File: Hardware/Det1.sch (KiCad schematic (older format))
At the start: 49 parts

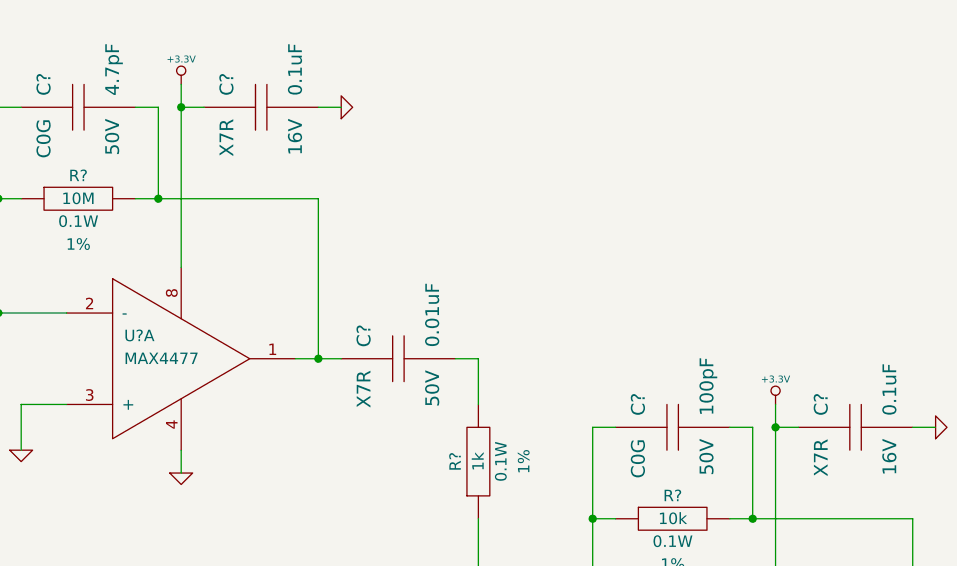
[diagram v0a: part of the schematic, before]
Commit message: Add LDO for analog
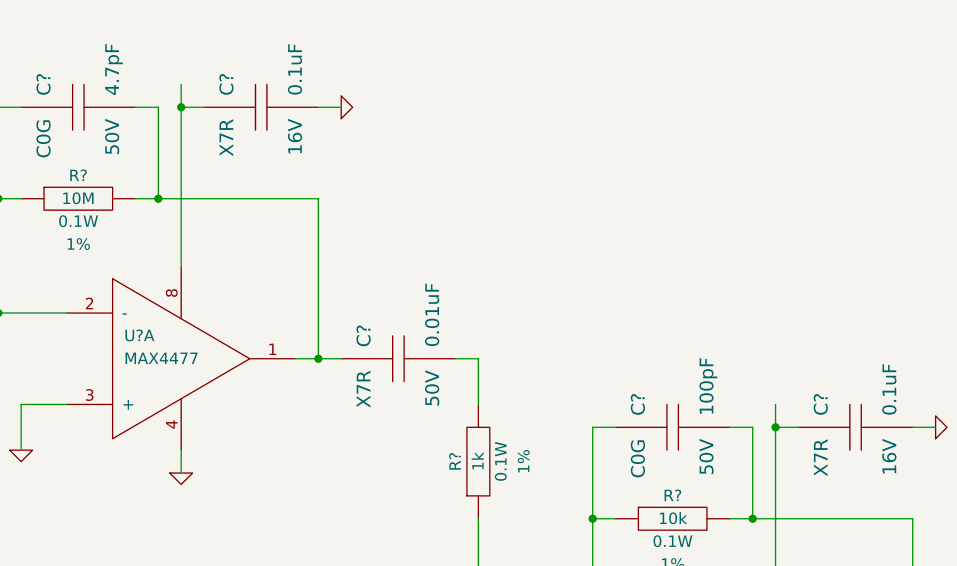
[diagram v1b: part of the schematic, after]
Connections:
- net labels removed: +3.3V
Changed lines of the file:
@@
 Sheet 2 5
 Title "Solid State Cosmic Ray Detector"
-Date "22 sep 2014"
+Date "23 sep 2014"
 Rev "1"
 Comp "Ethan Harstad"
@@
 $EndComp
 $Comp
-L +3.3V #PWR?
-U 1 1 52B91461
-P 6200 900
-F 0 "#PWR?" H 6200 860 30  0001 C CNN
-F 1 "+3.3V" H 6200 1010 30  0000 C CNN
-F 2 "" H 6200 900 60  0000 C CNN
-F 3 "" H 6200 900 60  0000 C CNN
-	1    6200 900
-	1    0    0    -1
-$EndComp
-$Comp
 L C C?
 U 1 1 52B91483
@@
 	0    -1   -1   0
 $EndComp
-$Comp
-L +3.3V #PWR?
-U 1 1 52B920B5
-P 8800 2300
-F 0 "#PWR?" H 8800 2260 30  0001 C CNN
-F 1 "+3.3V" H 8800 2410 30  0000 C CNN
-F 2 "" H 8800 2300 60  0000 C CNN
-F 3 "" H 8800 2300 60  0000 C CNN
-	1    8800 2300
-	1    0    0    -1
-$EndComp
-Wire Wire Line
+Wire Wire Line

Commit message: New detector chain
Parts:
- removed C? (x2): 4.7pF, CAPC1608, symbol C
- removed C? (x2): 0.1uF, CAPC1608, symbol C
- removed C? (x4): 0.01uF, CAPC1608, symbol C
- removed C? (x3): 100pF, CAPC1608, symbol C
- removed R? (x2): 10M, RESC1608, symbol R
- removed R? (x4): 1k, RESC1608, symbol R
- removed R? (x3): 10k, RESC1608, symbol R
- removed U? (x5): MAX4477, symbol OPAMP-DUAL
- added C? (x4): C, ~, symbol C
- added C? (x3): 0.1uF, CAPC1608, symbol C
- added C? (x2): 0.01uF, CAPC1608, symbol C
- added R? (x7): R, ~, symbol R
- added U? (x5): OPAMP-DUAL, ~, symbol OPAMP-DUAL
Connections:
- net labels added: VAA, VCOM
- net labels removed: +12V
- wire segments 116 -> 103
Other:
- note added: "Charge Amplifier"
- note added: "Differentiator Amplifier"
- note added: "Integrator Amplifier"

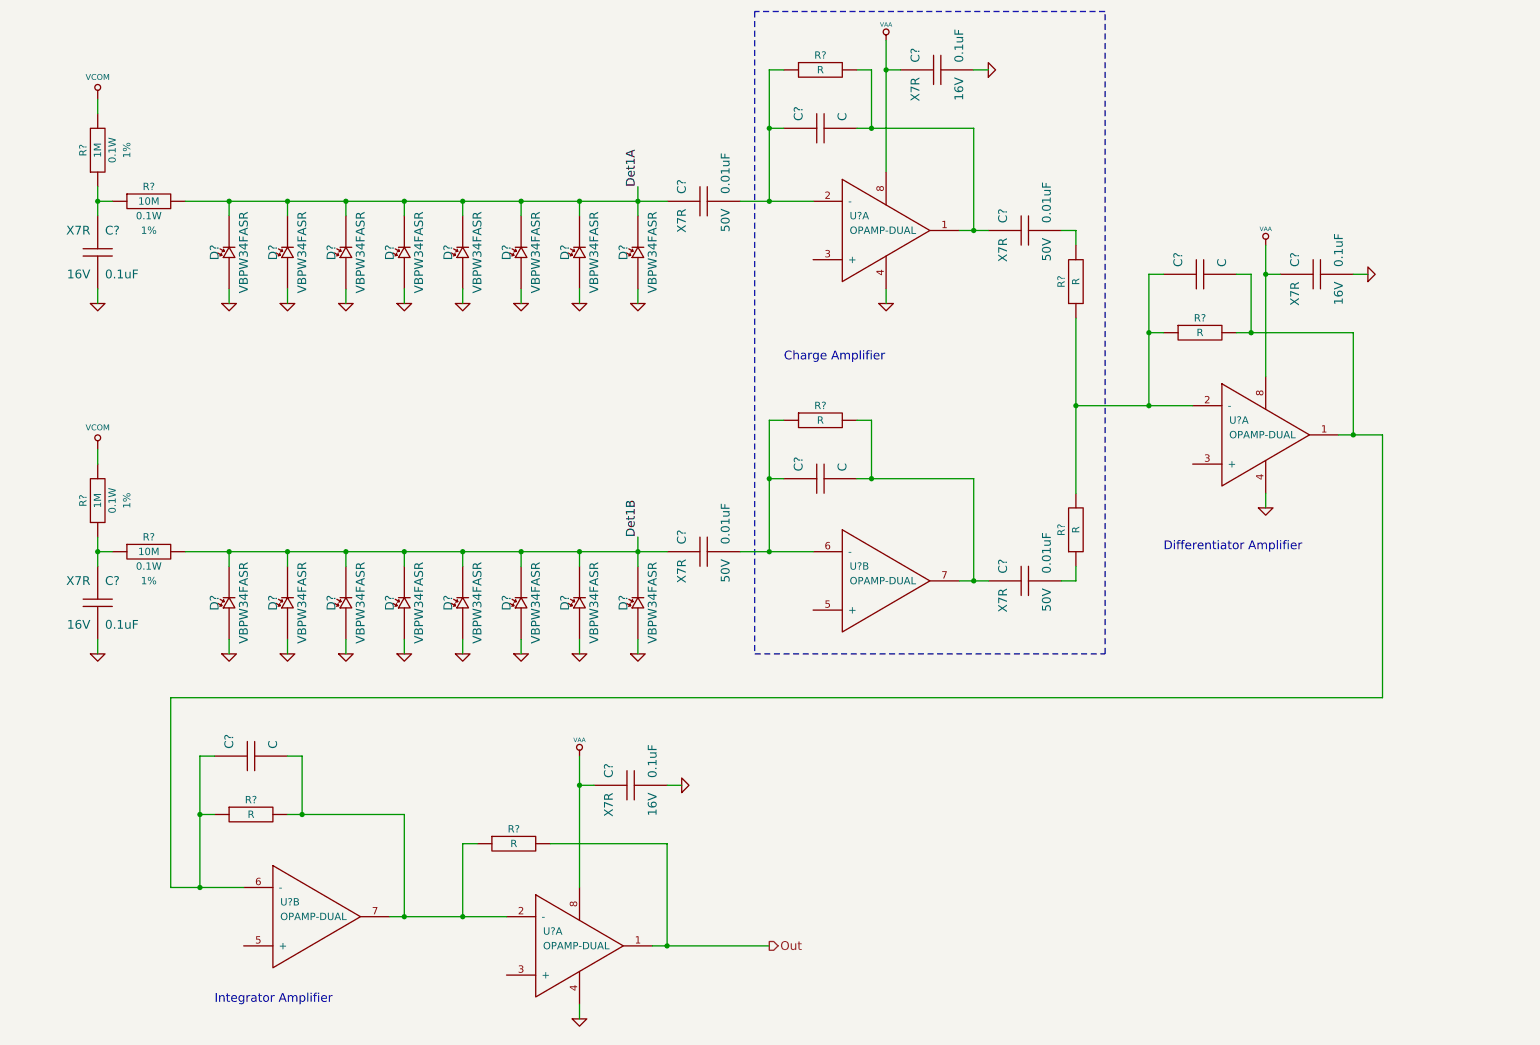
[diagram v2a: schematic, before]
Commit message: Rearrange detector chain
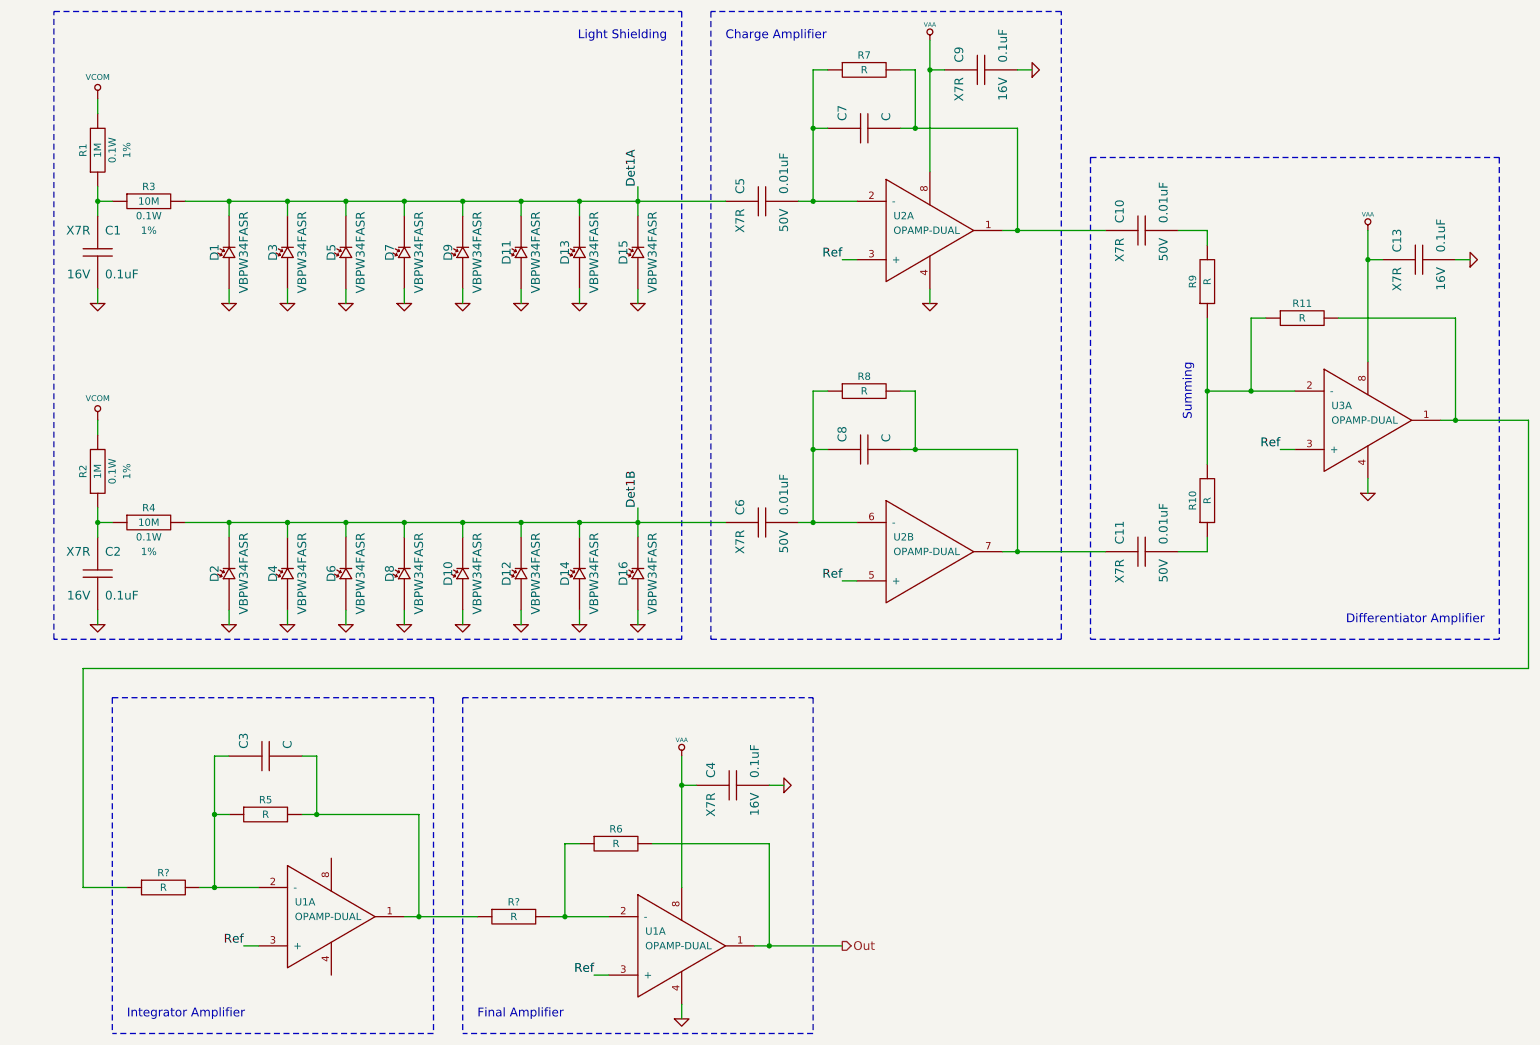
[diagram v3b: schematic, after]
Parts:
- removed C?: C, ~, symbol C
- added R? (x2): R, ~, symbol R
- gave numbers to parts that had none: 42
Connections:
- net Ref: now reaches U2.3 (+)
- net Ref: now also U1.3 (+), U1.3 (+), U2.5 (+), U3.3 (+)
- new net: R11.2, R?.1, U3.1
- new net: C3.2, R5.2, R?.1, U1.1
- new net: C3.1, R5.1, R?.2, U1.2 (-)
- new net: R6.1, R?.2, U1.2 (-)
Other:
- note added: "Final Amplifier"
- note added: "Light Shielding"
- note added: "Summing"
- moved on the sheet: C10, C11, C13, C2, C3, C4, C5, C6, C7, C8, C9, D10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

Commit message: Component values
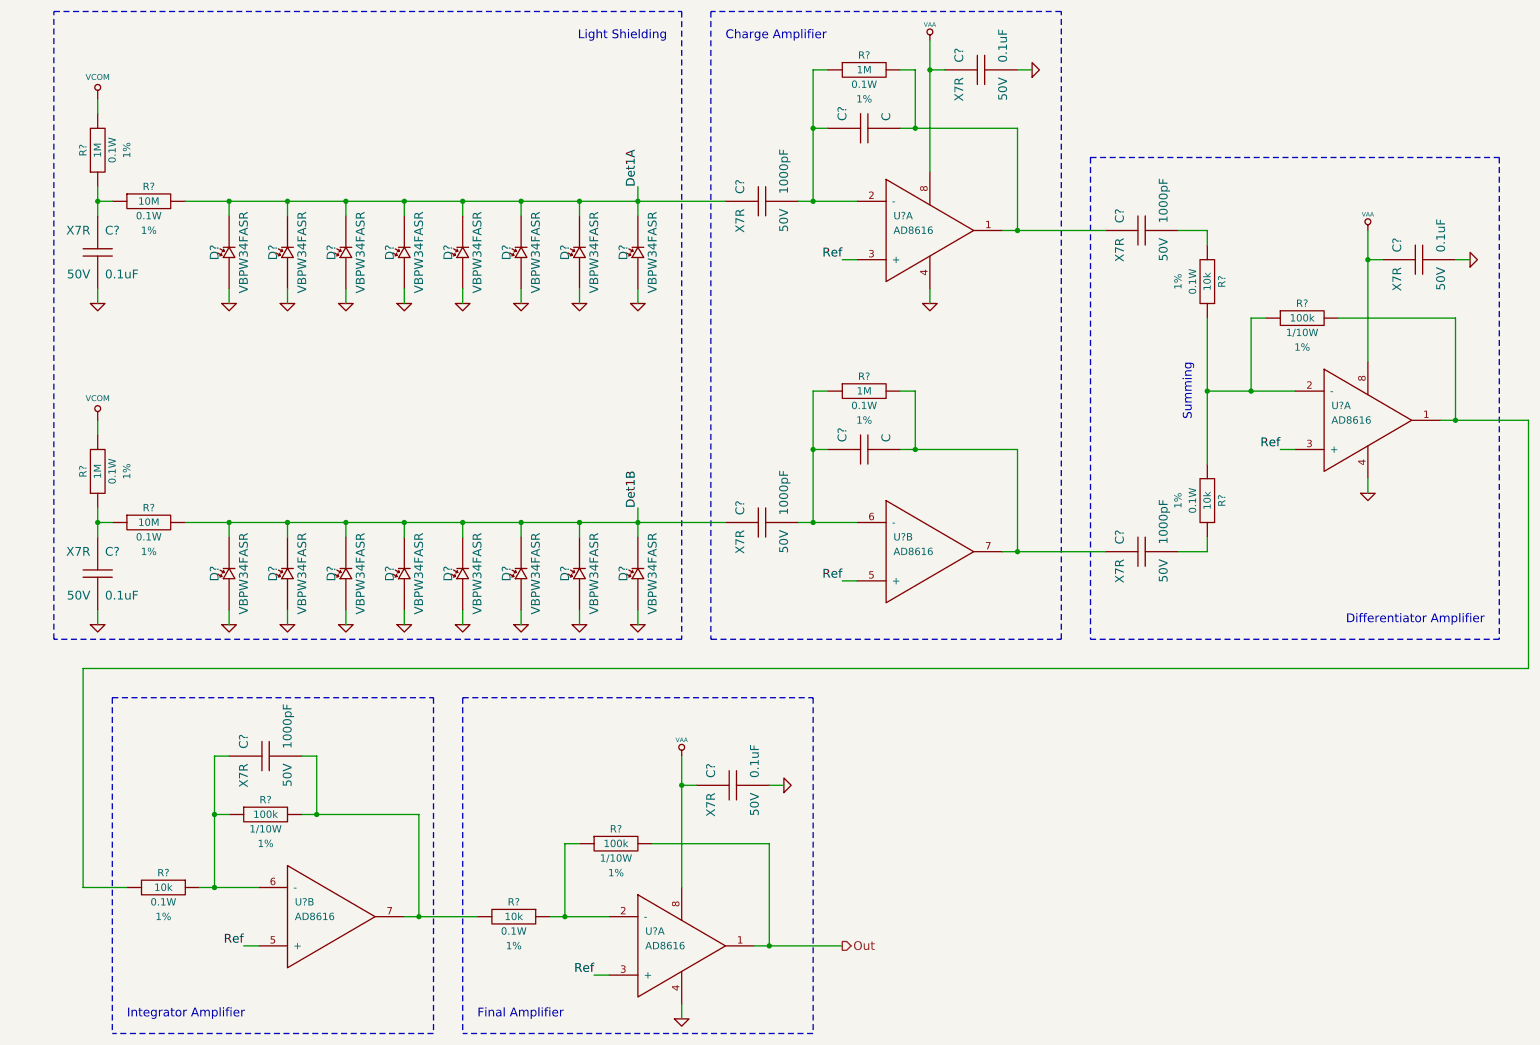
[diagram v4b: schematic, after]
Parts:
- removed C10, C11, C6: 0.01uF, CAPC1608, symbol C
- removed C13, C2, C4, C9: 0.1uF, CAPC1608, symbol C
- removed C3: C, ~, symbol C
- removed R10, R5, R6, R7, R8, R9, R? (x2): R, ~, symbol R
- removed U1 (x2), U3: OPAMP-DUAL, ~, symbol OPAMP-DUAL
- removed unit 2 of U2
- added C? (x4): 1000pF, CAPC1608, symbol C
- added C? (x4): 0.1uF, CAPC1608, symbol C
- added R? (x2): 1M, RESC1608, symbol R
- added R? (x4): 10k, RESC1608, symbol R
- added R? (x2): 100k, ~, symbol R
- added U? (x4): AD8616, ~, symbol OPAMP-DUAL
- C?: renamed from C1; Distributor Part No 1276-1005-1-ND -> 1276-1936-1-ND; MFR Part No CL10B104KO8NNNC -> CL10B104KB8SFNC; Voltage 16V -> 50V
- C?: renamed from C5; value 0.01uF -> 1000pF; Distributor Part No 1276-1921-1-ND -> 1276-1916-1-ND; MFR Part No CL10B103KB8NCNC -> CL10B102KB8SFNC
- R?: renamed from R11; value R -> 100k; Distributor Part No (none) -> 311-100KHRCT-ND; MFR Name (none) -> Yageo; MFR Part No (none) -> RC0603FR-07100KL; Power W -> 1/10W; Tolerance % -> 1%
- U?: renamed from U2; value OPAMP-DUAL -> AD8616; Distributor Part No (none) -> AD8616ARMZ-REELCT-ND; MFR Name (none) -> Analog; MFR Part No (none) -> AD8616ARMZ-REEL
- renumbered C7 to C?, C8 to C?, D15 to D?, D13 to D?, D11 to D?, D9 to D?, D7 to D?, D5 to D?, D3 to D?, D1 to D?, D16 to D?, D14 to D?, D12 to D?, D10 to D?, D8 to D?, D6 to D?, D4 to D?, D2 to D?, R1 to R?, R3 to R?, R4 to R?, R2 to R?
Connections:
- net Det1B: now also C?.1
- net GND: now also C?.2, C?.2, C?.2, C?.2, U?.4, U?.4
- net Out: now also R?.2, U?.1
- net Ref: now also U?.3 (+), U?.3 (+), U?.5 (+), U?.5 (+)
- net VAA: now also C?.1, C?.1, C?.1, U?.8, U?.8
- net at C?.1, C?.2, U?.2 (-): now also R?.1
- net at C?.1: now also C?.2, R?.1, U?.6 (-)
- net at R?.1, R?.1: now also C?.1
- net at C?.2, U?.1: now also C?.1, R?.2
- net at C?.2: now also C?.1, R?.2, U?.7
- net at R?.1: now also R?.1, R?.2, U?.2 (-)
- net at R?.2: now also R?.2, U?.1
- new net: C?.2, R?.2
- new net: C?.2, R?.1
- new net: C?.1, R?.1, R?.1, U?.6 (-)
- new net: C?.2, R?.2, R?.2, U?.7
- new net: R?.1, R?.1, U?.2 (-)
